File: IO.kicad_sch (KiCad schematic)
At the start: 10 parts, among them SW601 B3U-3100-P, U602 SN74LVC1G14DBVR

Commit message: Finished Everything
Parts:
- U602: footprint Package_TO_SOT_SMD:SOT-353_SC-70-5 -> Package_TO_SOT_SMD:SOT-23-5
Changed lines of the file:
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@@
 			)
 		)
-		(property "Footprint" "Package_TO_SOT_SMD:SOT-353_SC-70-5"
+		(property "Footprint" "Package_TO_SOT_SMD:SOT-23-5"
 			(at 114.3 59.69 0)
 			(effects

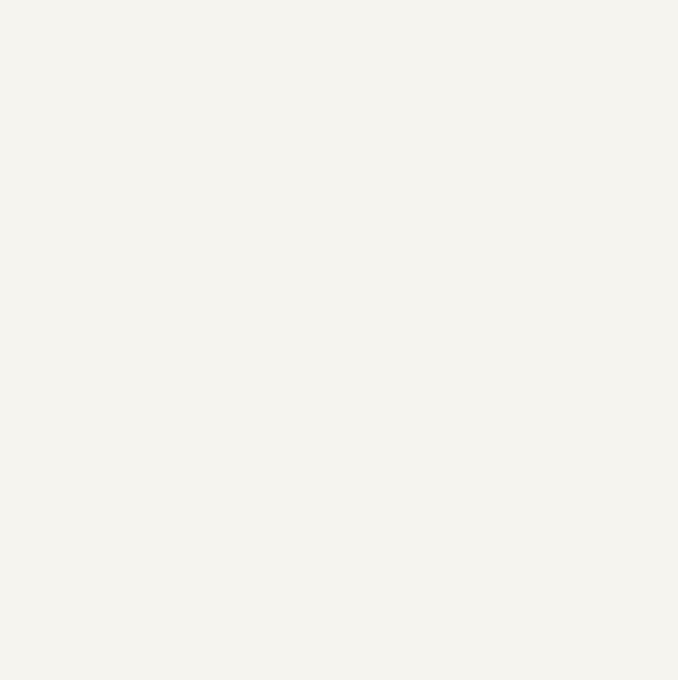
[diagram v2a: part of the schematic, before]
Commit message: Added Connector for Fan
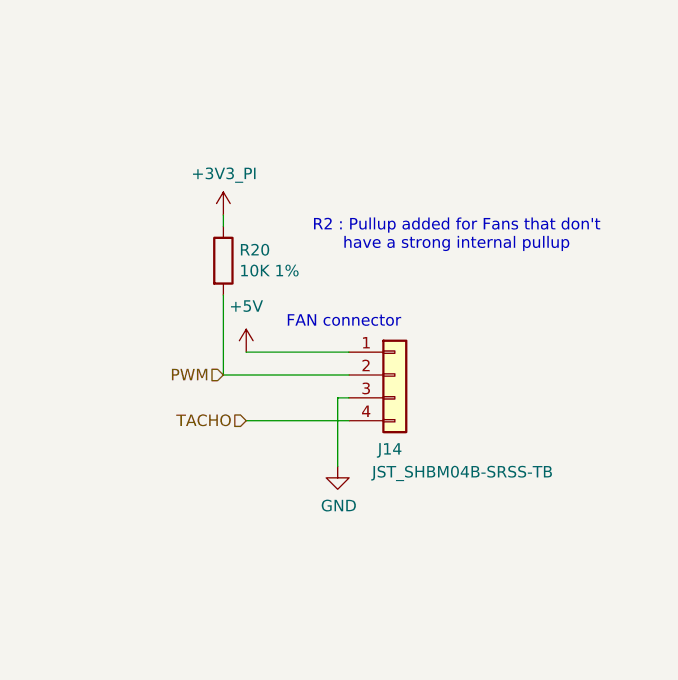
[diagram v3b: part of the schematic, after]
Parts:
- added J14: JST_SHBM04B-SRSS-TB, Connector_JST:JST_SH_BM04B-SRSS-TB_1x04-1MP_P1.00mm_Vertical, symbol Connector_Generic:Conn_01x04
- added R20: 10K 1%, Resistor_SMD:R_0402_1005Metric, symbol Device:R
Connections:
- net +3V3_PI: now also R20.1
- net +5V: now also J14.1 (Pin_1)
- net GND: now also J14.3 (Pin_3)
- new net PWM: J14.2 (Pin_2), R20.2
- new net TACHO: J14.4 (Pin_4)
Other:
- note added: "FAN connector"
- note added: "R2 : Pullup added for Fans that don't have a strong internal pullup"

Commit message: Made some changes
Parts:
- D605, D606: footprint Diode_SMD:D_0201_0603Metric_Pad0.64x0.40mm_HandSolder -> Diode_SMD:D_0805_2012Metric
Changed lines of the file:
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@@
 			)
 		)
-		(property "Footprint" "Diode_SMD:D_0201_0603Metric_Pad0.64x0.40mm_HandSolder"
+		(property "Footprint" "Diode_SMD:D_0805_2012Metric"
 			(at 176.53 46.99 0)
 			(hide yes)
@@
 			)
 		)
-		(property "Footprint" "Diode_SMD:D_0201_0603Metric_Pad0.64x0.40mm_HandSolder"
+		(property "Footprint" "Diode_SMD:D_0805_2012Metric"
 			(at 127 46.99 0)
 			(hide yes)
